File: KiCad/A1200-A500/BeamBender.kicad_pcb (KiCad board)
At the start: 4 copper layers, 50 x 100 mm, 74 parts, among them J1 4-1734742-0, J2 HDMI_A_1.4, J3 STX-3501-3N, J4 Phoenix_Contact, J5 Conn_01x01, J6 Conn_02x05_Odd_Even, U1 LM1117-3.3, U2 GW1NR-UV9LQ144P, U3 ADV7513BSWZ, U4 MCP1702T-1802E_CB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

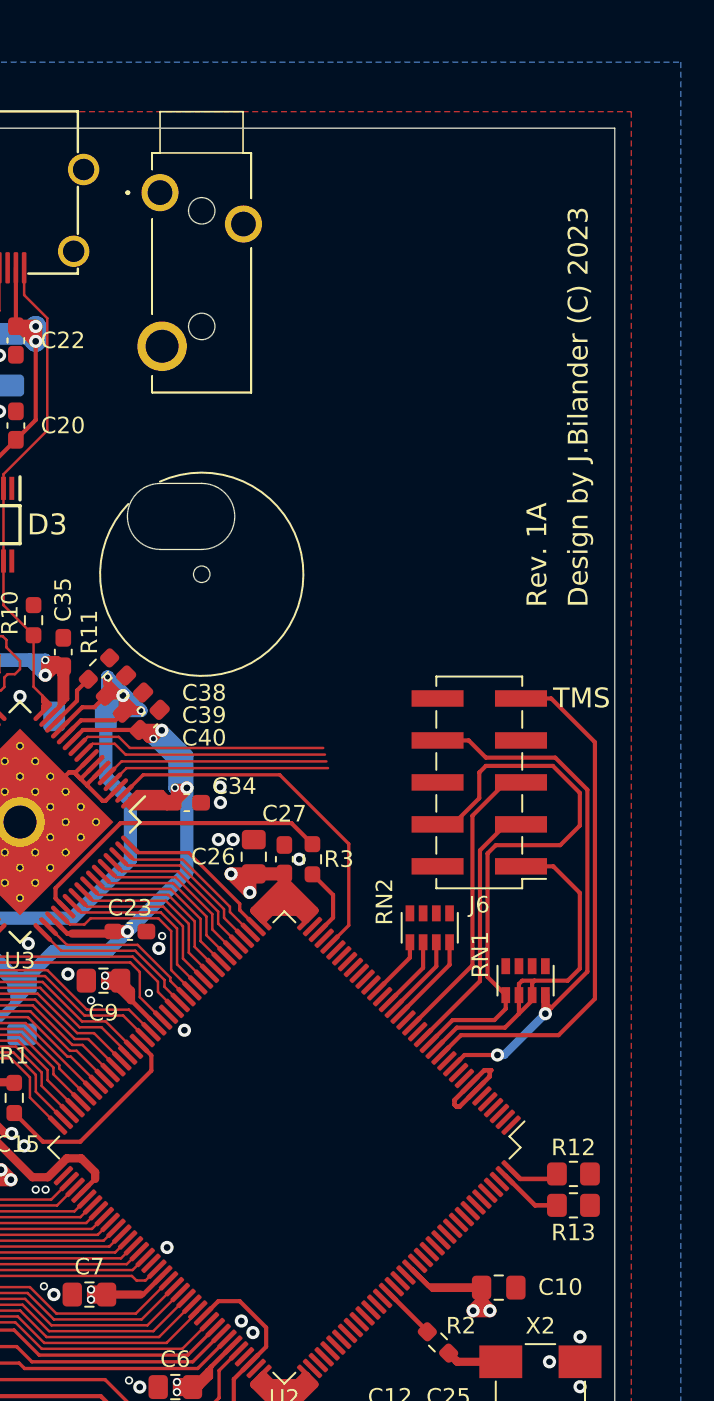
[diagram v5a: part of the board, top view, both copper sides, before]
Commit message: Fixed JTAG-connector and remaining 3V3-power routing and pull-ups for FPGA
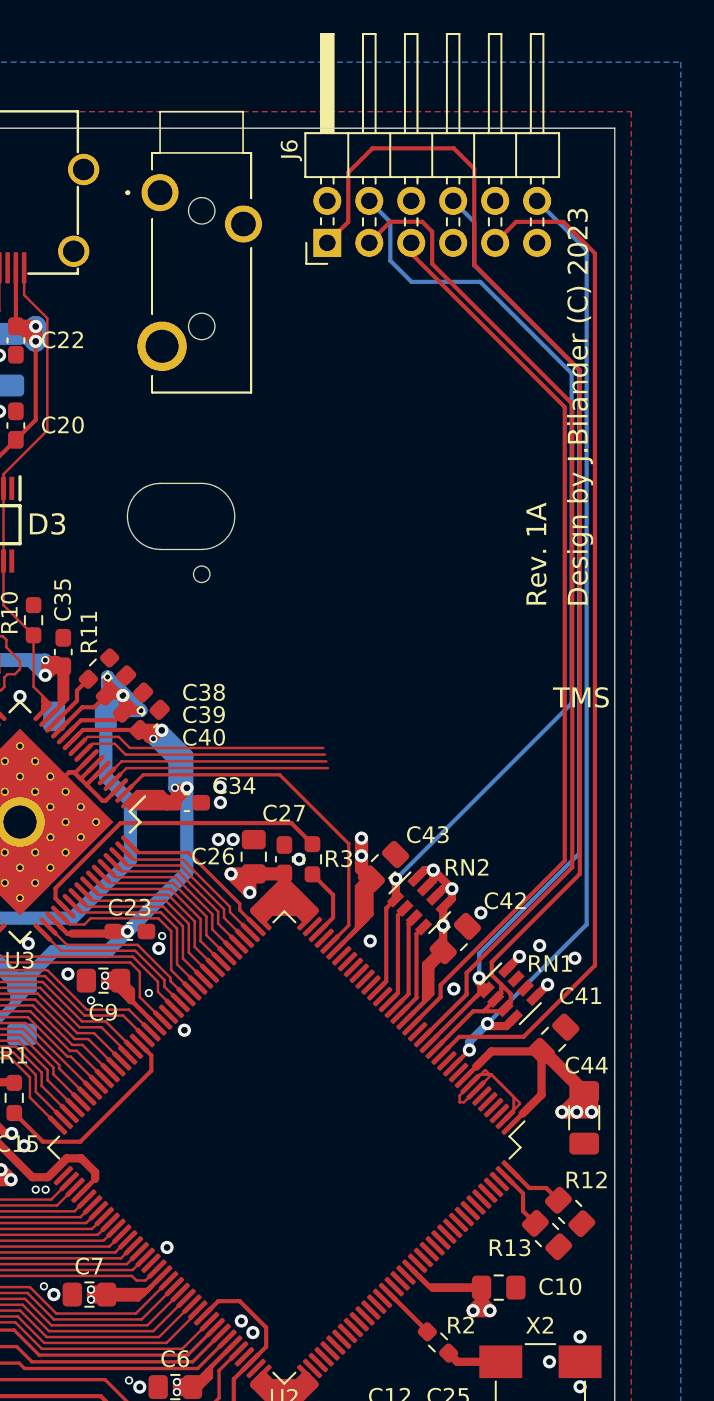
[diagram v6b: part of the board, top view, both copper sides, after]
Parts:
- added C41: 0.1uF, Capacitor_SMD:C_0805_2012Metric_Pad1.18x1.45mm_HandSolder, F.Cu at (144.4, 95.4)
- added C42: 0.1uF, Capacitor_SMD:C_0805_2012Metric_Pad1.18x1.45mm_HandSolder, F.Cu at (138.5, 89.3)
- added C43: 0.1uF, Capacitor_SMD:C_0805_2012Metric_Pad1.18x1.45mm_HandSolder, F.Cu at (134.1, 84.9)
- added C44: 10uF (1206), Capacitor_SMD:C_1206_3216Metric_Pad1.33x1.80mm_HandSolder, F.Cu at (146.3, 100.1)
- J6: value Conn_02x05_Odd_Even -> Conn_02x06_Odd_Even; footprint Connector_PinHeader_2.54mm:PinHeader_2x05_P2.54mm_Vertical_SMD -> Connector_PinHeader_2.54mm:PinHeader_2x06_P2.54mm_Horizontal
- moved J6 33.9 mm to (130.7, 47.2), turned to 90 degrees
- moved R13 2.41 mm to (144.0, 107.2), turned to 135 degrees
- moved R12 2.31 mm to (145.4, 105.8), turned to 135 degrees
- moved RN2 1.63 mm to (136.3, 87.1), turned to 45 degrees
- moved RN1 1.21 mm to (141.8, 92.6), turned to 45 degrees
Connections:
- RN1 pad 1: JP2 -> JP1
- RN1 pad 4: JP1 -> BT1
- RN2 pad 1: JP3 -> JP2
- U2 pad 11: JP1 -> BT1
- U2 pad 15: JP2 -> JP1
- U2 pad 24: JP3 -> JP2
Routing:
- net 3V3: track 219.3 -> 296.1 mm, vias 29 -> 39
- net BT1: track 0.00 -> 58.9 mm, vias 0 -> 2
- net TCK: track 23.0 -> 77.1 mm
- net TDI: track 15.9 -> 60.6 mm
- net TDO: track 18.0 -> 55.1 mm
- net TMS: track 31.8 -> 62.0 mm
- net JP1: track 33.9 -> 60.1 mm, vias 2 -> 1
- net JP2: track 35.3 -> 60.2 mm, vias 0 -> 1
- net GND: track 26.4 -> 38.8 mm, vias 71 -> 76
- net JP3: track 3.77 -> 0.00 mm
- net READY: track 4.52 -> 6.11 mm
- net DONE: track 5.06 -> 5.99 mm
- net MODE0: track 3.12 -> 3.63 mm

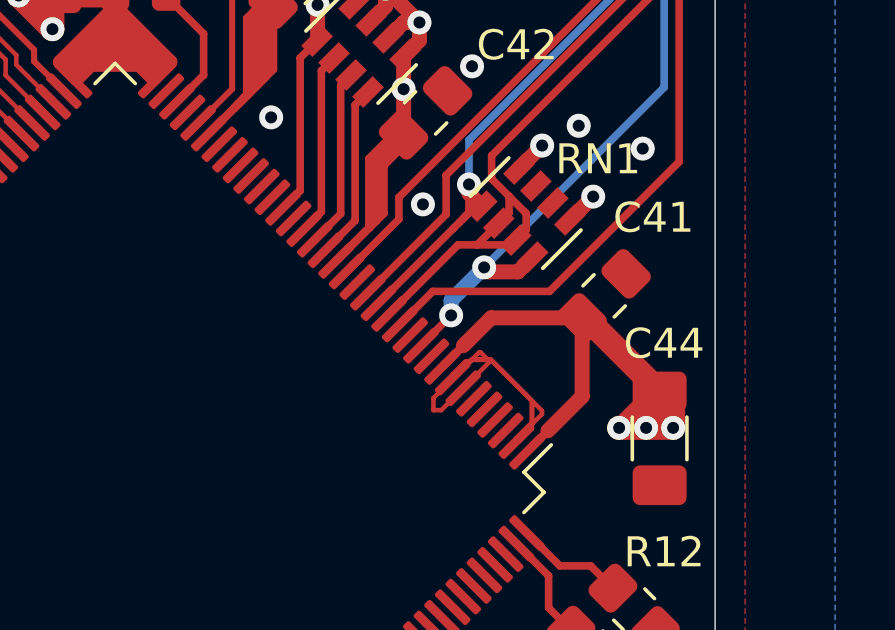
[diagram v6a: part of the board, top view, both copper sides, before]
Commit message: Added RC-debounce circuit to Button 1 (BT1)
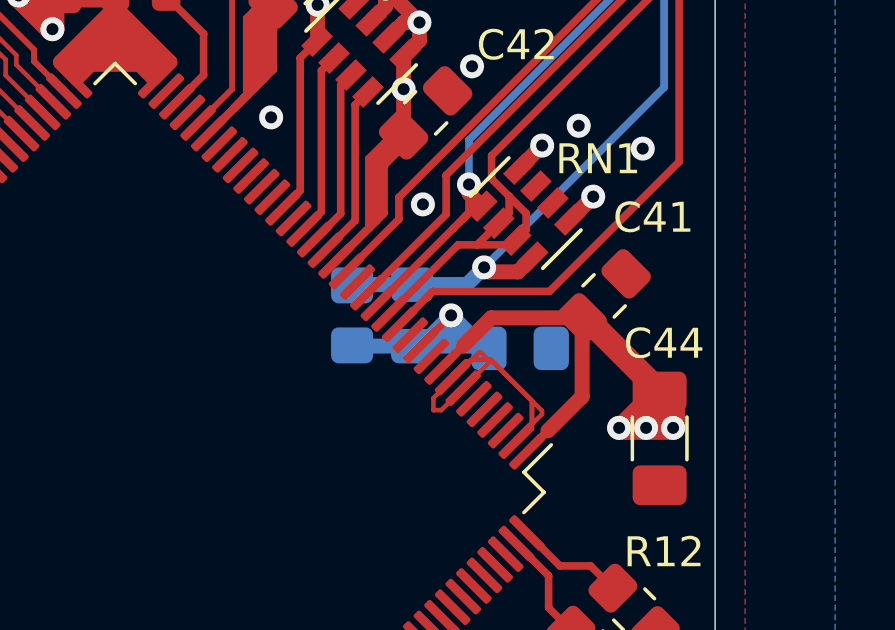
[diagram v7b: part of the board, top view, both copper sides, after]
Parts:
- added C45: 100nF (0805), Capacitor_SMD:C_0805_2012Metric_Pad1.18x1.45mm_HandSolder, B.Cu at (141.6, 97.1)
- added D4: D_Small, Diode_SMD:D_0805_2012Metric_Pad1.15x1.40mm_HandSolder, B.Cu at (138.0, 96.0)
- added R14: 10k, Resistor_SMD:R_0805_2012Metric_Pad1.20x1.40mm_HandSolder, B.Cu at (136.0, 96.0)
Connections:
- U2 pad 11: BT1 -> Net-(C45-Pad1)
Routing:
- net Net-(C45-Pad1): track 0.00 -> 12.7 mm, vias 0 -> 1
- net BT1: track 58.9 -> 60.1 mm, vias 2 -> 1

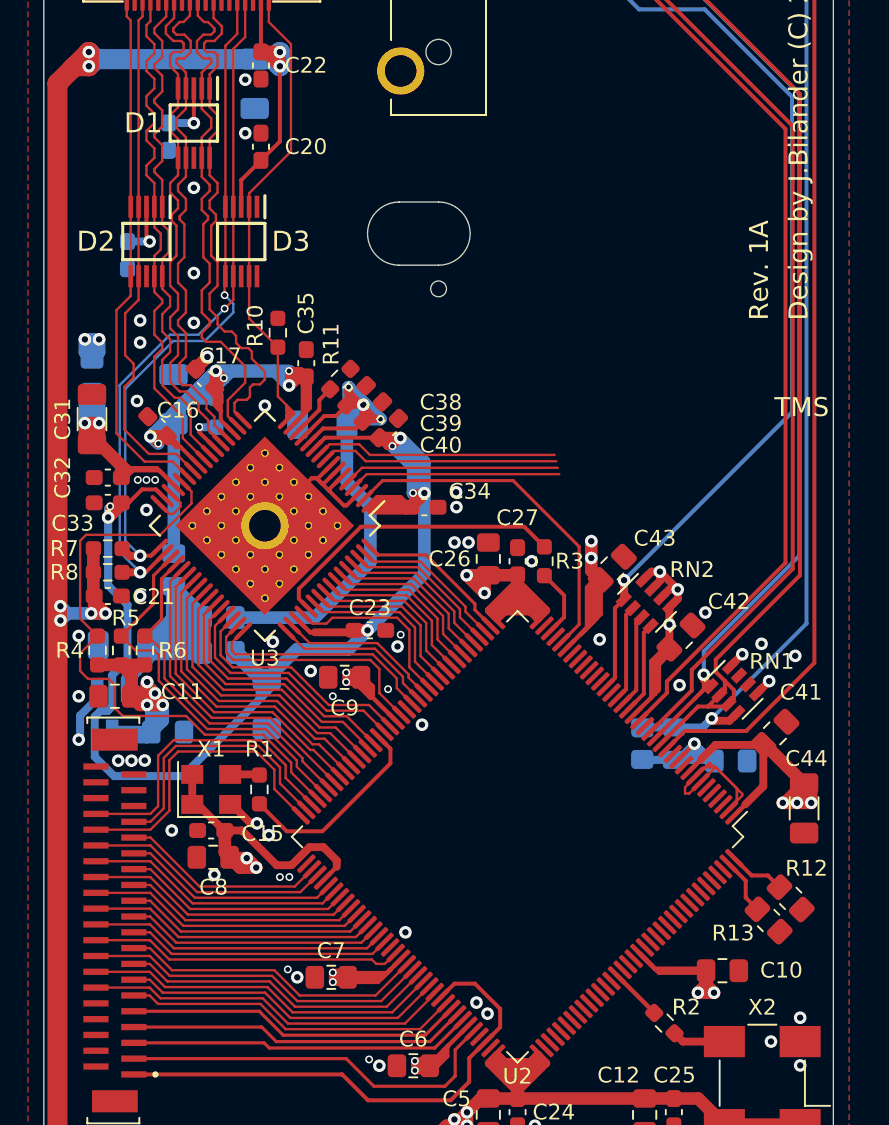
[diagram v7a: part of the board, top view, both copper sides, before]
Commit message: Added ADC-chip AK5720VT
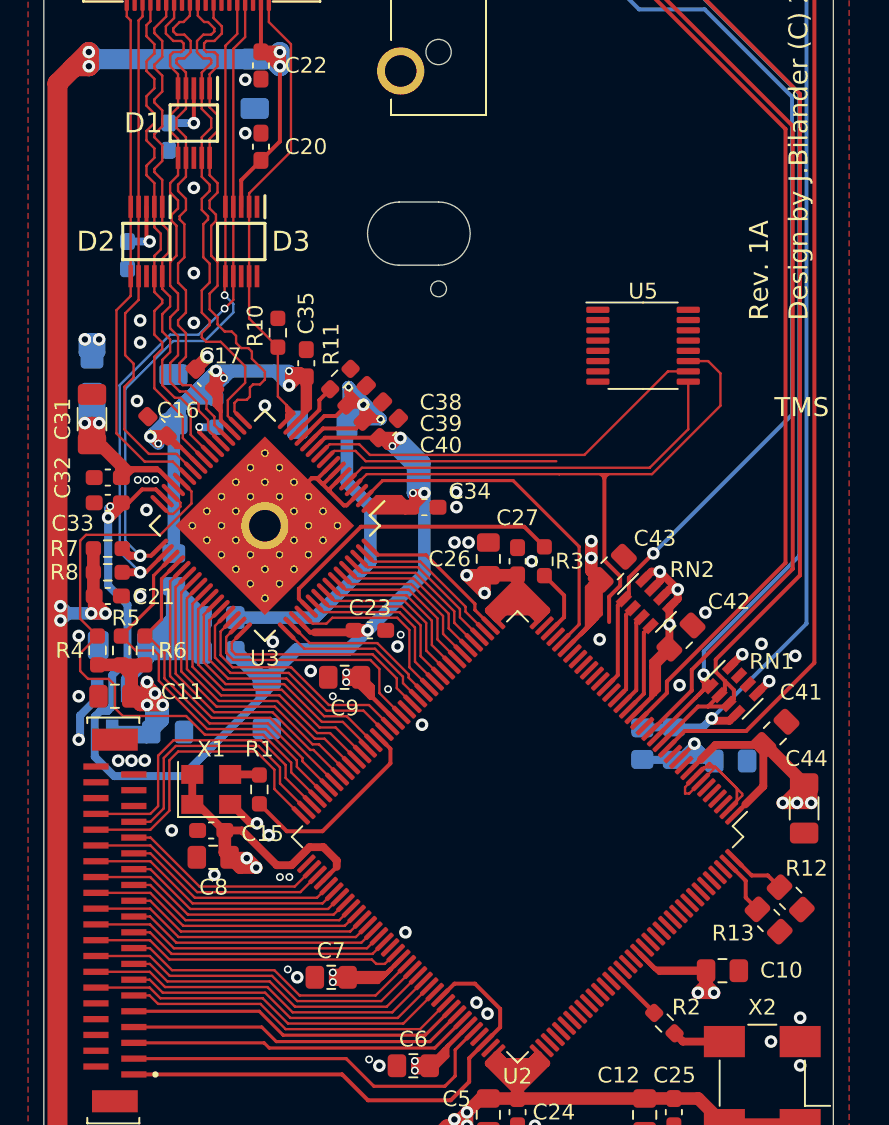
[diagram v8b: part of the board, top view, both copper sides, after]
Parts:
- added U5: AK5720VT, Package_SO:TSSOP-16_4.4x5mm_P0.65mm, F.Cu at (136.1, 70.8)
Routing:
- net MCLK: track 13.4 -> 40.8 mm
- net I2S0: track 13.6 -> 25.9 mm
- net LRCLK: track 15.4 -> 26.0 mm
